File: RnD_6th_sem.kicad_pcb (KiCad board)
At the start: 2 copper layers, 41 parts, among them Q1 IGLD60R190D1, Q2 IGLD60R190D1, U1 2EDF7275K

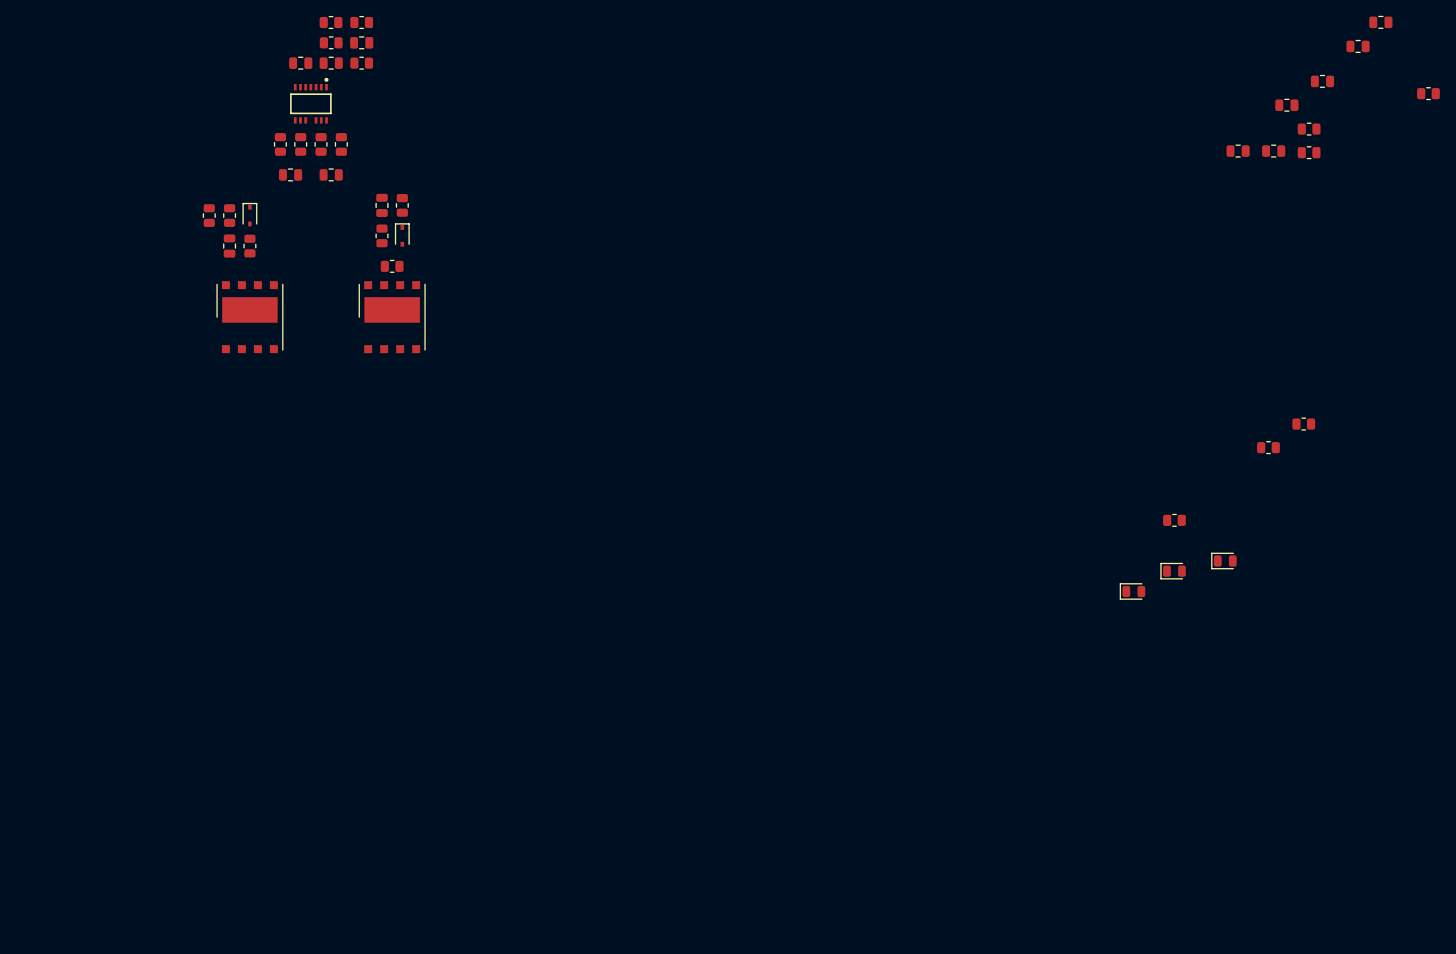
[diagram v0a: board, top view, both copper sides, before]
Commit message: added current sense resistors
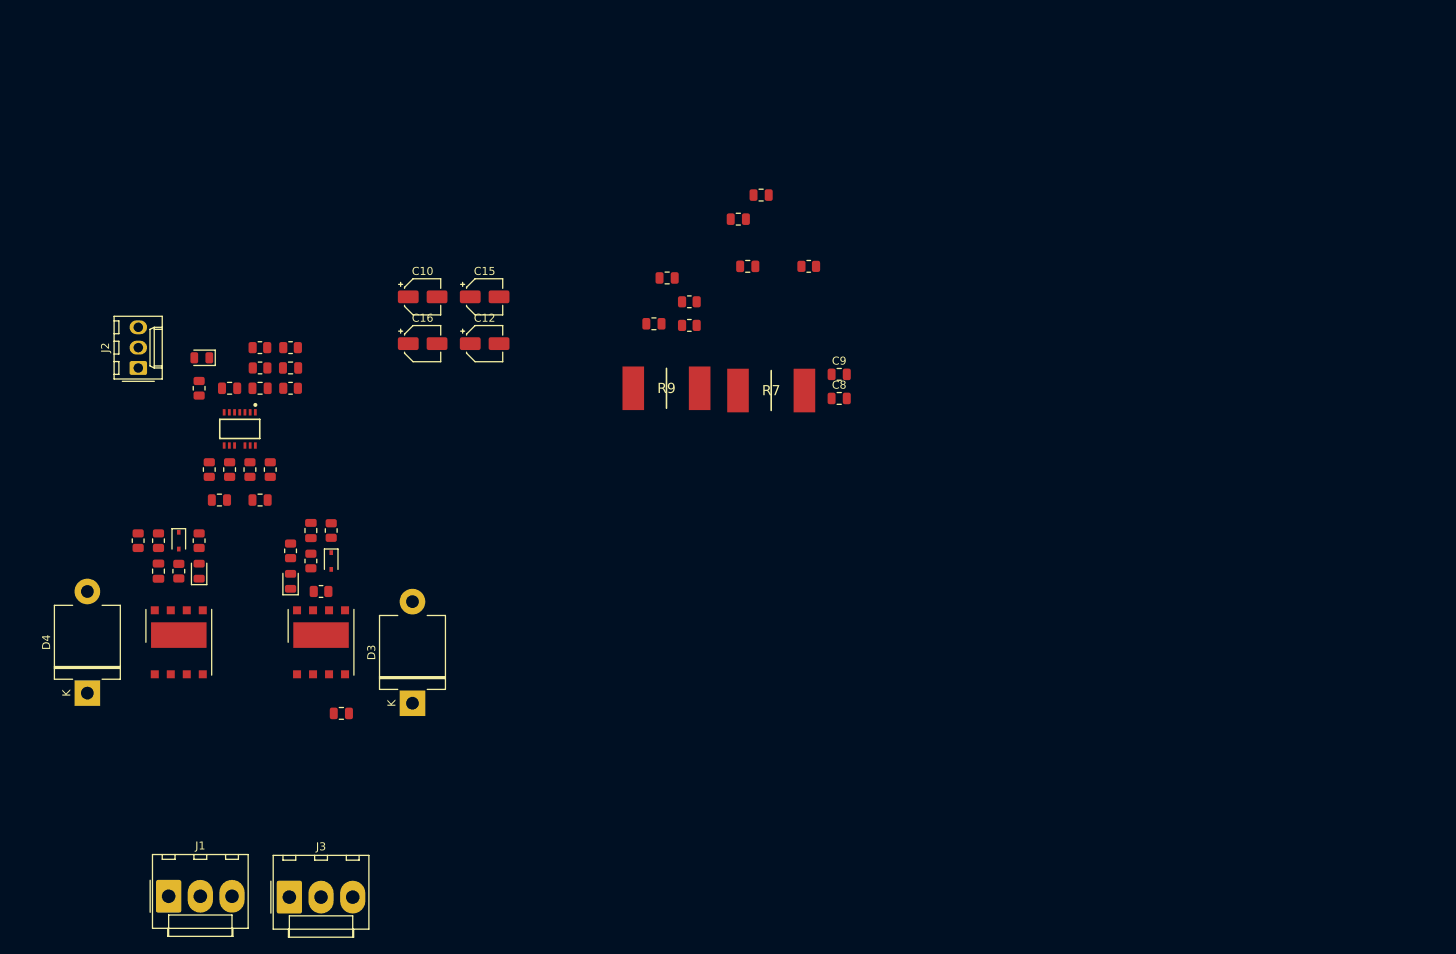
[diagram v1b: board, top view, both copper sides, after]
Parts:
- added C10: 100uF/250V, Capacitor_SMD:CP_Elec_4x5.8, F.Cu at (97.8, 52.1)
- added C12: 100uF/250V, Capacitor_SMD:CP_Elec_4x5.8, F.Cu at (105.5, 57.9)
- added C15: 10uF/35V, Capacitor_SMD:CP_Elec_4x5.8, F.Cu at (105.5, 52.1)
- added C16: 10uF/35V, Capacitor_SMD:CP_Elec_4x5.8, F.Cu at (97.8, 57.9)
- added C8: 100nF/100V, Capacitor_SMD:C_0805_2012Metric, F.Cu at (149.9, 64.8)
- added C9: 100nF/100V, Capacitor_SMD:C_0805_2012Metric, F.Cu at (149.9, 61.8)
- added D3: D_Schottky, Diode_THT:D_5KPW_P12.70mm_Horizontal, F.Cu at (96.5, 102.9)
- added D4: D_Schottky, Diode_THT:D_5KPW_P12.70mm_Horizontal, F.Cu at (55.9, 101.6)
- added J1: HVDC1, Connector_Molex:Molex_KK-396_A-41791-0003_1x03_P3.96mm_Vertical, F.Cu at (66.0, 127.0)
- added J2: PWM, Connector_Molex:Molex_KK-254_AE-6410-03A_1x03_P2.54mm_Vertical, F.Cu at (62.2, 61.0)
- added J3: HVDC2, Connector_Molex:Molex_KK-396_A-41791-0003_1x03_P3.96mm_Vertical, F.Cu at (81.1, 127.1)
- added R7: WSLP3921L1000FEA, footprint:RESC10052X50N, F.Cu at (141.4, 63.8)
- added R9: WSLP3921L1000FEA, footprint:RESC10052X50N, F.Cu at (128.3, 63.5)
- C6, C7: value 10nF -> 100nF/100V
- moved R11 138.8 mm to (69.8, 82.5), turned to 90 degrees
- moved C9 132.3 mm to (87.6, 104.1)
- moved D5 130.4 mm to (70.2, 59.7), turned to 180 degrees
- moved R10 123.0 mm to (69.8, 63.5), turned to -90 degrees
- moved R12 122.9 mm to (81.3, 83.8), turned to 90 degrees
- moved D6 121.9 mm to (69.8, 86.4), turned to 90 degrees
- moved D7 105.4 mm to (81.3, 87.6), turned to 90 degrees
- moved C10 80.4 mm to (137.2, 42.4)
- moved C11 80.4 mm to (140.1, 39.4)
- moved C7 80.4 mm to (128.3, 49.7)
- moved R7 80.4 mm to (131.1, 55.6)
- moved R8 80.4 mm to (131.1, 52.7)
- moved R9 80.4 mm to (146.1, 48.3)
- moved C8 80.4 mm to (126.7, 55.4)
- moved C6 75.5 mm to (138.4, 48.3)
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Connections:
- net Net-(C4-Pad1) renamed /OUTA
- net Net-(D1-Pad1) renamed /OUTAB
- C6 pad 1: Net-(C10-Pad1) -> Net-(C10-Pad2)
- C7 pad 1: Net-(C10-Pad1) -> Net-(C10-Pad2)
- Q1 pad 1: Net-(C10-Pad2) -> Net-(D3-Pad1)
- Q1 pad 2: Net-(C10-Pad2) -> Net-(D3-Pad1)
- Q1 pad 3: Net-(C10-Pad2) -> Net-(D3-Pad1)
- Q1 pad 4: Net-(C10-Pad2) -> Net-(D3-Pad1)
- Q2 pad 5: Net-(C10-Pad1) -> Net-(D4-Pad2)
- Q2 pad 6: Net-(C10-Pad1) -> Net-(D4-Pad2)
- Q2 pad 9: Net-(C10-Pad1) -> Net-(D4-Pad2)

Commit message: updated the schematic
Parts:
- removed D3, D4: D_Schottky, Diode_THT:D_5KPW_P12.70mm_Horizontal
- added J4: 3.3V, Connector_Molex:Molex_KK-254_AE-6410-02A_1x02_P2.54mm_Vertical, F.Cu at (162.7, 69.5)
- added REF**: TestPoint_2Pads_Pitch2.54mm_Drill0.8mm, TestPoint:TestPoint_2Pads_Pitch2.54mm_Drill0.8mm, F.Cu at (48.3, 72.4)
- added REF**: TestPoint_2Pads_Pitch2.54mm_Drill0.8mm, TestPoint:TestPoint_2Pads_Pitch2.54mm_Drill0.8mm, F.Cu at (48.3, 78.7)
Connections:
- net /OUTA renamed OUTA
- net /OUTAB renamed OUTB
- net /pwm1 renamed PWM1
- net /pwm2 renamed PWM2
- C10 pad 1: Net-(C10-Pad1) -> HVDC+
- C10 pad 2: Net-(C10-Pad2) -> GND3
- C12 pad 1: Net-(C10-Pad1) -> HVDC+
- C12 pad 2: Net-(C10-Pad2) -> GND3
- C15 pad 1: VCCA -> Net-(U1-Pad13)
- C15 pad 2: GNDA -> Net-(C15-Pad2)
- C16 pad 1: VCCB -> Net-(C16-Pad1)
- C16 pad 2: GNDB -> Net-(C16-Pad2)
- C2 pad 1: GNDA -> Net-(C15-Pad2)
- C2 pad 2: VCCA -> Net-(U1-Pad13)
- C3 pad 1: GNDB -> Net-(C16-Pad2)
- C3 pad 2: VCCB -> Net-(C16-Pad1)
- C6 pad 1: Net-(C10-Pad2) -> GND3
- C7 pad 1: Net-(C10-Pad2) -> GND3
- C8 pad 2: Net-(C10-Pad1) -> HVDC+
- C9 pad 2: Net-(C10-Pad1) -> HVDC+
- D6 pad 1: GNDB -> GND1
- D7 pad 1: GNDA -> GND2
- FB3 pad 2: VCCA -> VCCB
- FB4 pad 2: VCCB -> VCCA
- J1 pad 2: Net-(C10-Pad2) -> GND3
- J1 pad 3: Net-(C10-Pad1) -> HVDC+
- J3 pad 2: Net-(C10-Pad2) -> GND3
- J3 pad 3: Net-(C10-Pad1) -> HVDC+
- Q1 pad 7: GNDA -> GND1
- Q2 pad 7: GNDB -> GND2
- R11 pad 2: VCCB -> VCCA
- R12 pad 2: VCCA -> VCCB
- R7 pad 2: Net-(C10-Pad1) -> HVDC+
- R9 pad 2: Net-(C10-Pad2) -> GND3
- U1 pad 10: Net-(FB4-Pad1) -> Net-(C16-Pad1)
- U1 pad 11: Net-(FB2-Pad1) -> Net-(C15-Pad2)
- U1 pad 13: Net-(FB3-Pad1) -> Net-(U1-Pad13)
- U1 pad 8: Net-(FB1-Pad1) -> Net-(C16-Pad2)
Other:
- copper layers 2 -> 4

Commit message: after ubuntu push
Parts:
- removed the C10 at (137.2, 42.4)
- removed the C10 at (97.8, 52.1)
- removed C11, C9: 1uF/400-450V, Capacitor_SMD:C_0805_2012Metric
- removed C12: 100uF/250V, Capacitor_SMD:CP_Elec_4x5.8
- removed C6, C7, C8, C9: 100nF/100V, Capacitor_SMD:C_0805_2012Metric
- removed C8: 10nF, Capacitor_SMD:C_0805_2012Metric
- removed FB1, FB2: fb, Resistor_SMD:R_0805_2012Metric
- removed the R7 at (141.4, 63.8)
- removed the R7 at (131.1, 55.6)
- removed the R9 at (128.3, 63.5)
- removed the R9 at (146.1, 48.3)
- added C10: 220uF/450V, Capacitor_SMD:CP_Elec_4x5.8, F.Cu at (129.5, 95.2)
- added R17: 1R, Resistor_SMD:R_0805_2012Metric, F.Cu at (124.5, 86.4)
- added R18: 1R, Resistor_SMD:R_0805_2012Metric, F.Cu at (134.6, 86.4)
- added R19: 1R, Resistor_SMD:R_0805_2012Metric, F.Cu at (132.1, 86.4)
- added R20: 1R, Resistor_SMD:R_0805_2012Metric, F.Cu at (121.9, 86.4)
- added R21: NC, Resistor_SMD:R_0805_2012Metric, F.Cu at (127.0, 86.4)
- added R22: NC, Resistor_SMD:R_0805_2012Metric, F.Cu at (129.5, 86.4)
- added R7: WSLP3921L1000FEA, footprint:RESC10052X50N, F.Cu at (143.5, 86.4)
- added R9: WSLP3921L1000FEA, footprint:RESC10052X50N, F.Cu at (113.0, 86.4)
- Q1, Q2: moved to B.Cu
- R8: value 10 -> 500k
- moved FB4 75.2 mm to (146.1, 53.3), turned to 0 degrees
- moved FB3 70.9 mm to (146.1, 51.3), turned to 0 degrees
- moved J2 68.3 mm to (130.2, 53.9), turned to 0 degrees
- moved D6 67.9 mm to (137.2, 77.5)
- moved R11 67.9 mm to (137.2, 73.7)
- moved C5 63.1 mm to (127.0, 76.2), turned to -90 degrees
- moved R2 63.1 mm to (127.0, 72.4)
- moved R3 63.1 mm to (124.5, 72.4)
- moved REF** 62.8 mm to (109.2, 57.1)
- moved J3 60.7 mm to (137.3, 104.0), turned to 180 degrees
- moved R14 60.6 mm to (137.9, 61.5), turned to 180 degrees
- moved J1 60.4 mm to (121.9, 104.1), turned to 180 degrees
- moved REF** 59.9 mm to (104.1, 57.1)
- moved Q2 57.0 mm to (123.7, 86.4), turned to -90 degrees
- moved R16 57.0 mm to (134.4, 61.5), turned to 180 degrees
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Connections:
- C13 pad 2: PWM1 -> PWM2
- C14 pad 2: PWM2 -> PWM1
- C15 pad 1: Net-(U1-Pad13) -> LED1
- C16 pad 1: Net-(C16-Pad1) -> LED2
- C2 pad 2: Net-(U1-Pad13) -> LED1
- C3 pad 2: Net-(C16-Pad1) -> LED2
- R11 pad 2: VCCA -> LED1
- R12 pad 2: VCCB -> LED2
- R13 pad 2: PWM1 -> PWM2
- R14 pad 2: PWM2 -> PWM1
- R15 pad 1: PWM1 -> PWM2
- R16 pad 1: PWM2 -> PWM1
- R8 pad 1: Net-(C7-Pad2) -> HVDC+
- R8 pad 2: Net-(C10-Pad2) -> GND3
- U1 pad 10: Net-(C16-Pad1) -> LED2
- U1 pad 13: Net-(U1-Pad13) -> LED1

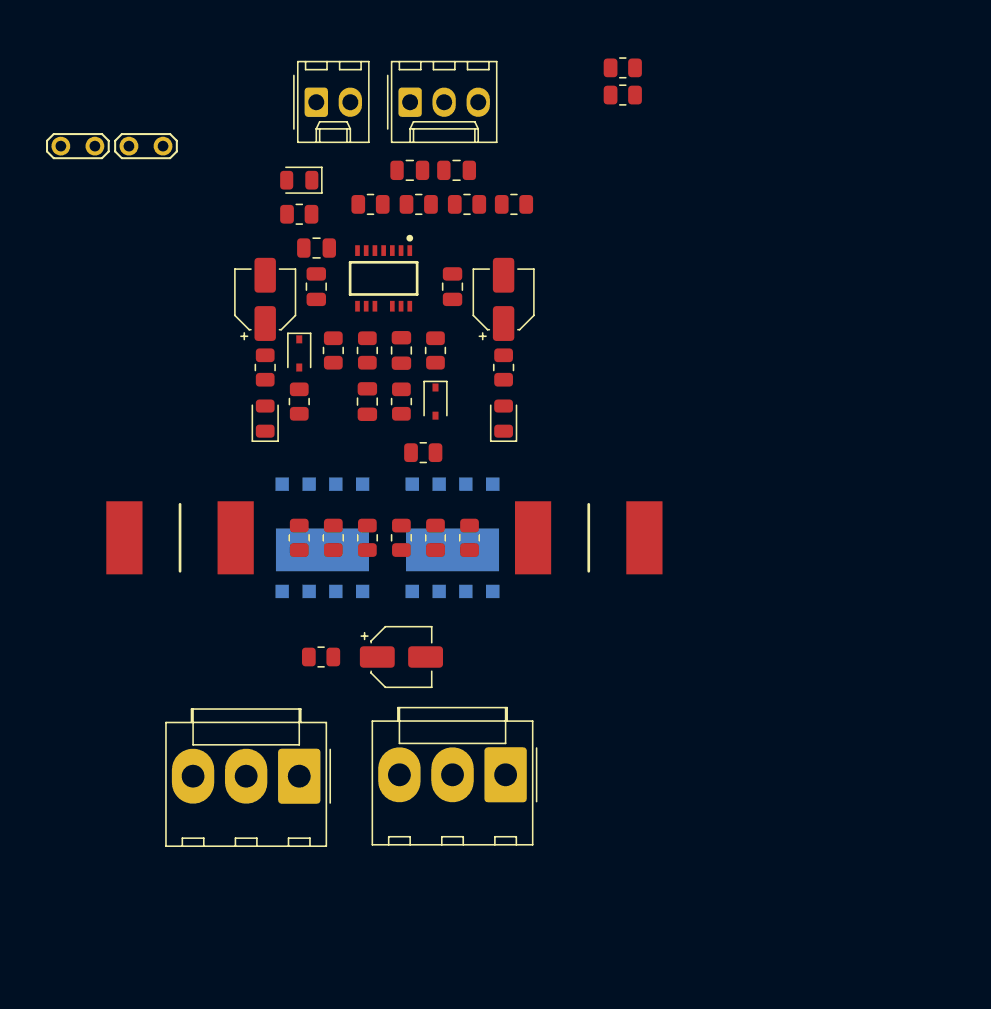
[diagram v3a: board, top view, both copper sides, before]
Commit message: changed GD Symbol
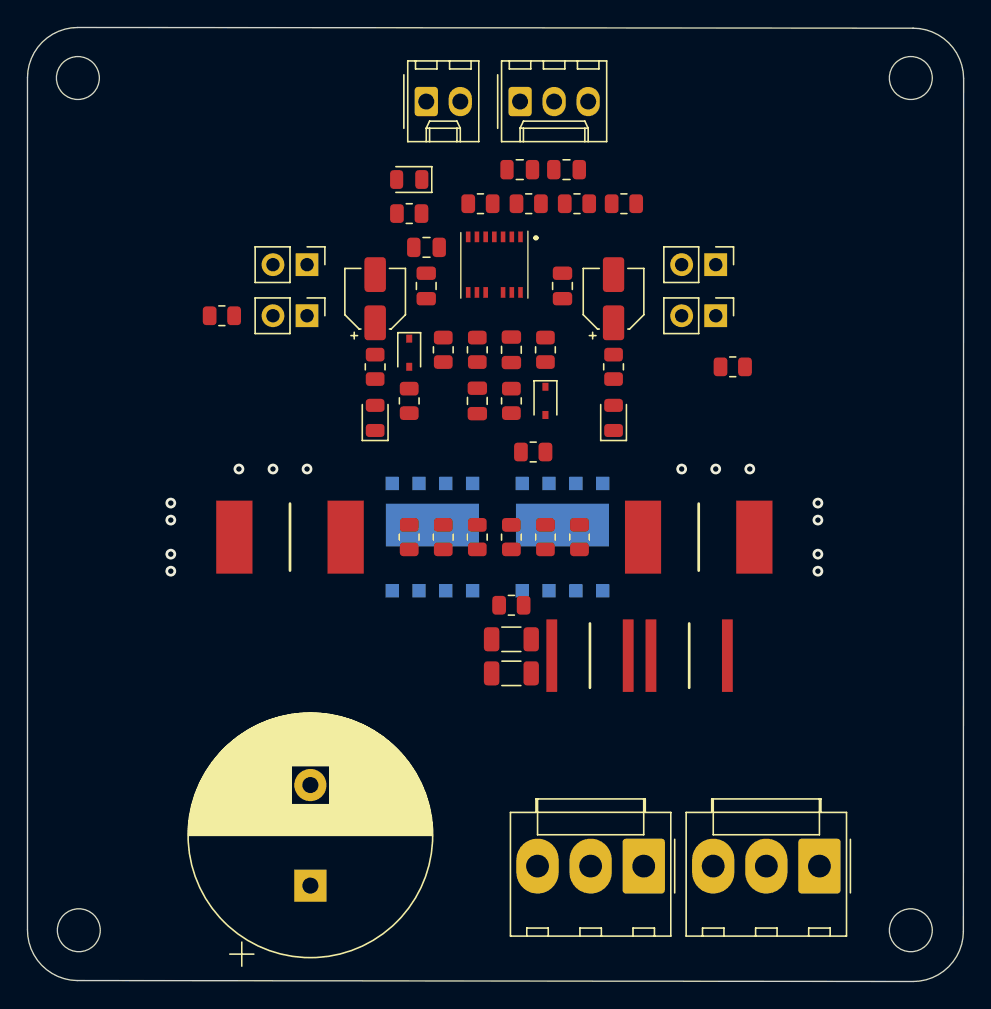
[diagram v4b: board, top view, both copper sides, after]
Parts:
- removed REF** (x2): TestPoint_2Pads_Pitch2.54mm_Drill0.8mm, TestPoint:TestPoint_2Pads_Pitch2.54mm_Drill0.8mm
- removed U1: 2EDF7275K, footprint:TFLGA65P500X500X106-14_13N-V
- added C6: 100nF/630V, Capacitor_SMD:C_1206_3216Metric, F.Cu at (137.7, 93.9)
- added C7: 100nF/630V, Capacitor_SMD:C_1206_3216Metric, F.Cu at (137.7, 96.5)
- added C8: 1uF/450V, CGA9P4X7T2W105K250KA:CAPC5750X280N, F.Cu at (143.6, 95.2)
- added C9: 1uF/450V, CGA9P4X7T2W105K250KA:CAPC5750X280N, F.Cu at (151.0, 95.2)
- added H1: MountingHole, MountingHole:MountingHole_3.2mm_M3, F.Cu at (167.5, 115.6)
- added H2: MountingHole, MountingHole:MountingHole_3.2mm_M3, F.Cu at (105.5, 115.6)
- added H3: MountingHole, MountingHole:MountingHole_3.2mm_M3, F.Cu at (167.5, 52.1)
- added H4: MountingHole, MountingHole:MountingHole_3.2mm_M3, F.Cu at (105.4, 52.1)
- added IC1: 2EDF7275KXUMA1, 2EDF7275KXUMA1:2EDF7275KXUMA1, F.Cu at (136.5, 66.0)
- added J5: 5V, Connector_PinHeader_2.54mm:PinHeader_1x02_P2.54mm_Vertical, F.Cu at (153.0, 69.8)
- added J6: 5V, Connector_PinHeader_2.54mm:PinHeader_1x02_P2.54mm_Vertical, F.Cu at (122.5, 69.8)
- added J7: GND2, Connector_PinHeader_2.54mm:PinHeader_1x02_P2.54mm_Vertical, F.Cu at (122.5, 66.0)
- added J8: GND1, Connector_PinHeader_2.54mm:PinHeader_1x02_P2.54mm_Vertical, F.Cu at (153.0, 66.0)
- C10: value 220uF/450V -> 100uF/450V; footprint Capacitor_SMD:CP_Elec_4x5.8 -> Capacitor_THT:CP_Radial_D18.0mm_P7.50mm
- moved J1 39.4 mm to (160.7, 110.8)
- moved FB3 35.2 mm to (116.2, 69.8)
- moved FB4 21.9 mm to (154.2, 73.6)
- moved C10 18.4 mm to (122.8, 112.3), turned to 90 degrees
- moved R8 14.7 mm to (137.7, 91.4)
- moved J3 12.3 mm to (147.6, 110.8)
- moved C15 8.20 mm to (145.4, 68.5)
- moved C2 8.20 mm to (141.6, 67.6)
- moved C4 8.20 mm to (137.7, 72.3)
- moved D6 8.20 mm to (145.4, 77.4)
- moved Q1 8.20 mm to (141.6, 86.3), turned to 90 degrees
- moved R11 8.20 mm to (145.4, 73.6)
- moved R13 8.20 mm to (135.4, 61.4)
- moved R15 8.20 mm to (139.0, 61.4)
- moved R16 8.20 mm to (142.6, 61.4)
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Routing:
- net (no net): vias 0 -> 14
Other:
- board outline added: 69.8 x 71.1 mm
